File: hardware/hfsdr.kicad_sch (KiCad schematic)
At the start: 57 parts, among them J1 USB_C_Receptacle_USB2.0_16P, SW1 RST, SW2 BOOT0, SW4 RotaryEncoder_Switch, U3 CH32V30xRxTx

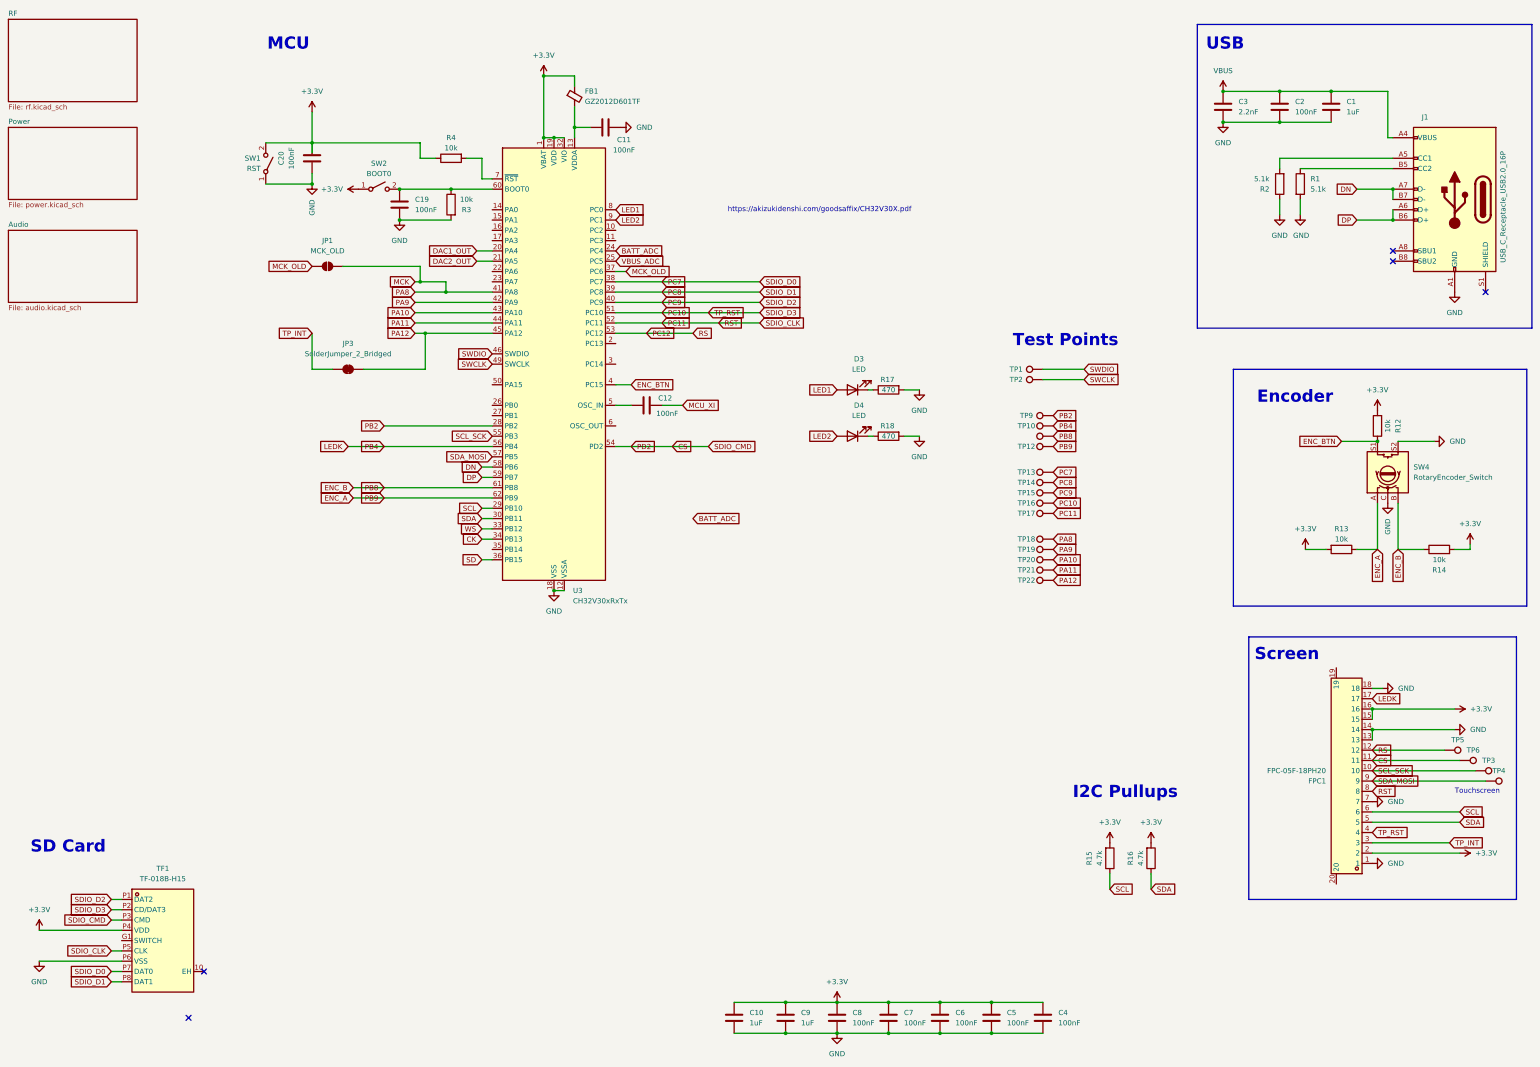
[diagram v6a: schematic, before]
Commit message: feat: tf card slot and screen rerouting
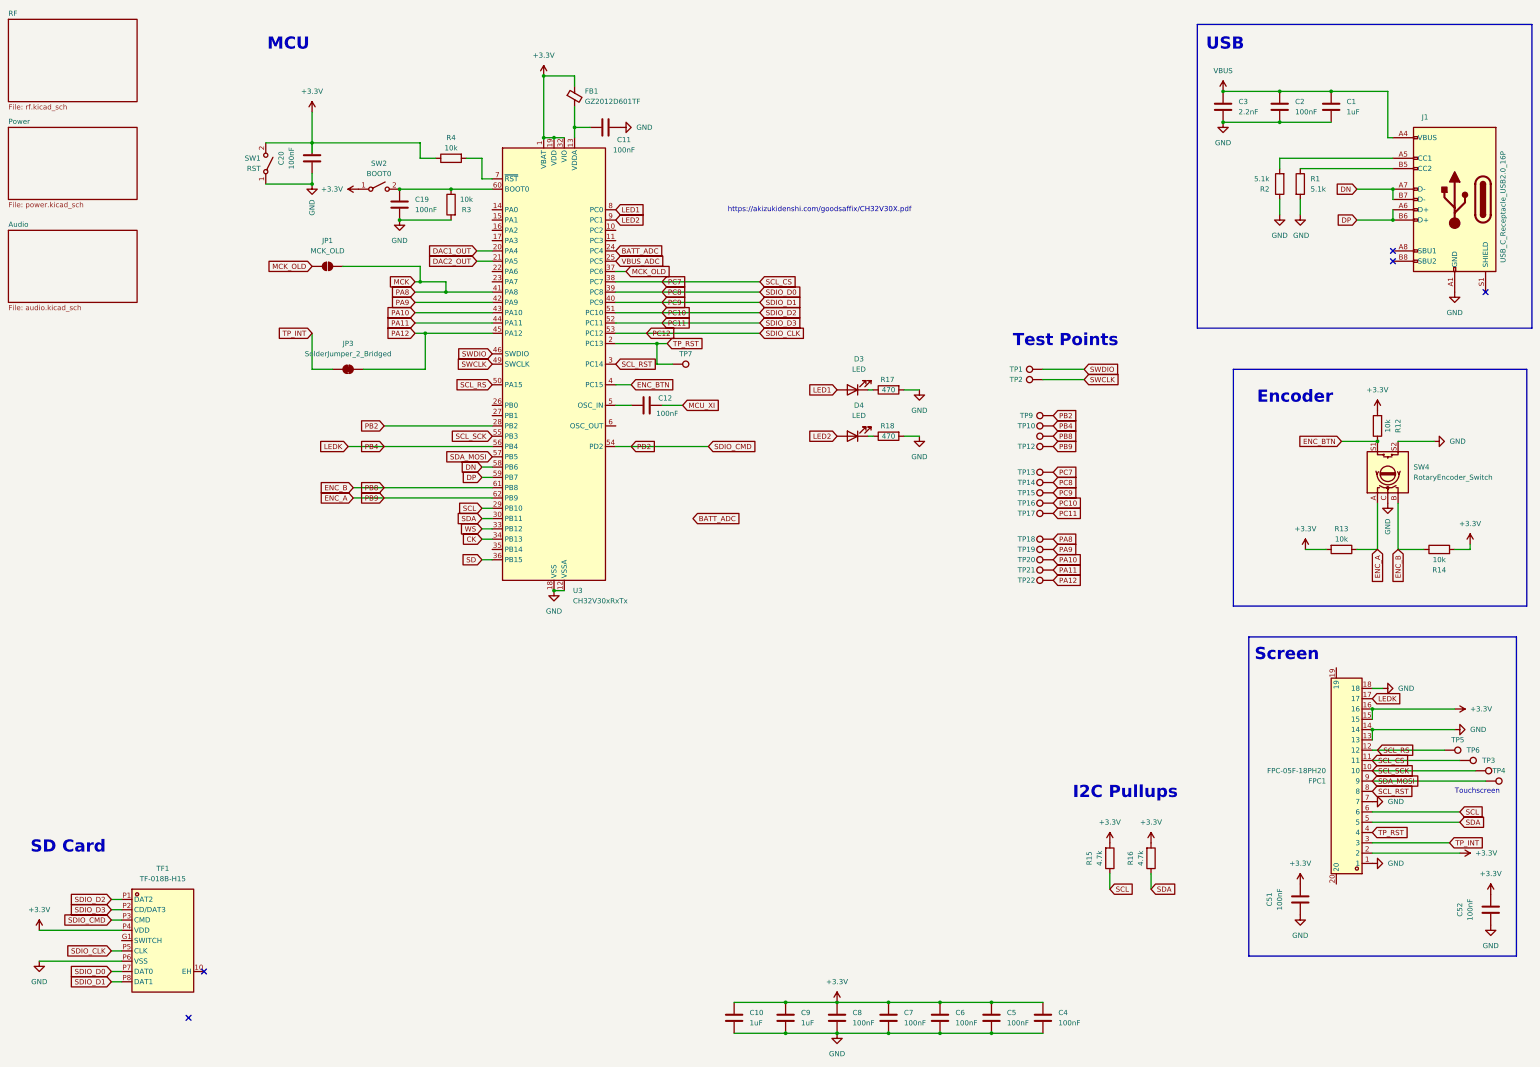
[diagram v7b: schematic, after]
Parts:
- added C51, C52: 100nF, Capacitor_SMD:C_0805_2012Metric_Pad1.18x1.45mm_HandSolder, symbol Device:C
- added TP7: TestPoint, TestPoint:TestPoint_Pad_1.0x1.0mm, symbol Connector:TestPoint
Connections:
- net +3.3V: now also C51.2, C52.2
- net GND: now also C51.1, C52.1
- net PC10: now also TF1.P1 (DAT2); no longer FPC1.4, TF1.P2 (CD/DAT3)
- net PC11: now also TF1.P2 (CD/DAT3); no longer FPC1.8, TF1.P5 (CLK)
- net PC12: now also TF1.P5 (CLK); no longer FPC1.12, TP5.1
- net PC7: now also FPC1.11, TP6.1; no longer TF1.P7 (DAT0)
- net PC8: now also TF1.P7 (DAT0); no longer TF1.P8 (DAT1)
- net PC9: now also TF1.P8 (DAT1); no longer TF1.P1 (DAT2)
- net TP_RST: now reaches U3.2 (PC13)
- net TP_RST: now also FPC1.4, TP7.1
- net SCL_RST: now reaches U3.3 (PC14)
- net SCL_RST: now also FPC1.8
- net SCL_RS: now reaches U3.50 (PA15)
- net SCL_RS: now also FPC1.12, TP5.1
- net CS renamed PD2
- net PD2: no longer FPC1.11, TP6.1

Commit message: Ready for production
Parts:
- added C53: 1uF, Capacitor_SMD:C_0805_2012Metric_Pad1.18x1.45mm_HandSolder, symbol Device:C
- added C54: 100nF, Capacitor_SMD:C_0805_2012Metric_Pad1.18x1.45mm_HandSolder, symbol Device:C
- C3: value 2.2nF -> 10nF
- R15, R16: value 4.7k -> 2k
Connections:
- net GND: now also C53.1, C54.1
- net VBUS: now also C53.2, C54.2
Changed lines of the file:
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@@
 	)
 	(junction
+		(at 345.44 30.48)
+		(diameter 0)
+		(color 0 0 0 0)
+	)
+	(junction
 		(at 332.74 38.1)
 		(diameter 0)
@@
 	(wire
 		(pts
+			(xy 332.74 30.48) (xy 345.44 30.48)
+		)
+		(stroke
+			(width 0)
+			(type default)
+		)
+	)
+	(wire
+		(pts
 			(xy 44.45 242.57) (xy 46.99 242.57)
 		)
@@
 			)
 		)
-		(property "Value" "4.7k"
+		(property "Value" "2k"
 			(at 298.45 227.33 90)
 			(effects
@@
 	)
 	(symbol
+		(lib_id "Device:C")
+		(at 345.44 34.29 0)
+		(unit 1)
+		(exclude_from_sim no)
+		(in_bom yes)
+		(on_board yes)
+		(dnp no)
+		(fields_autoplaced yes)
+		(property "Reference" "C53"
+			(at 349.25 33.0199 0)
+			(effects
+				(font
+					(size 1.27 1.27)
+				)
+				(justify left)
+			)
+		)
+		(property "Value" "1uF"
+			(at 349.25 35.5599 0)
+			(effects
+				(font
+					(size 1.27 1.27)
+				)
+				(justify left)
+			)
+		)
+		(property "Footprint" "Capacitor_SMD:C_0805_2012Metric_Pad1.18x1.45mm_HandSolder"
+			(at 346.4052 38.1 0)
+			(effects
+				(font
+					(size 1.27 1.27)
+				)
+				(hide yes)
+			)
+		)
+		(property "Datasheet" "~"
+			(at 345.44 34.29 0)
+			(effects
+				(font
+					(size 1.27 1.27)
+				)
+				(hide yes)
+			)
+		)
+		(property "Description" "Unpolarized capacitor"
+			(at 345.44 34.29 0)
+			(effects
+				(font
+					(size 1.27 1.27)
+				)
+				(hide yes)
+			)
+		)
+		(pin "2"
+		)
+		(pin "1"
+		)
+		(instances
+			(project "hfsdr"
+				(path "/a11445ed-c3bd-4d1c-a039-1c09b0dceab8"
+					(reference "C53")
+					(unit 1)
+				)
+			)
+		)
+	)
+	(symbol
 		(lib_id "Connector:TestPoint")
 		(at 276.86 120.65 90)
@@
 			)
 		)
-		(property "Value" "4.7k"
+		(property "Value" "2k"
 			(at 288.29 227.33 90)
 			(effects
@@
 	)
 	(symbol
+		(lib_id "power:GND")
+		(at 345.44 30.48 180)
+		(unit 1)
+		(exclude_from_sim no)
+		(in_bom yes)
+		(on_board yes)
+		(dnp no)
+		(fields_autoplaced yes)
+		(property "Reference" "#PWR089"
+			(at 345.44 24.13 0)
+			(effects
+				(font
+					(size 1.27 1.27)
+				)
+				(hide yes)
+			)
+		)
+		(property "Value" "GND"
+			(at 345.44 25.4 0)
+			(effects
+				(font
+					(size 1.27 1.27)
+				)
+			)
+		)
+		(property "Footprint" ""
+			(at 345.44 30.48 0)
+			(effects
+				(font
+					(size 1.27 1.27)
+				)
+				(hide yes)
+			)
+		)
+		(property "Datasheet" ""
+			(at 345.44 30.48 0)
+			(effects
+				(font
+					(size 1.27 1.27)
+				)
+				(hide yes)
+			)
+		)
+		(property "Description" "Power symbol creates a global label with name \"GND\" , ground"
+			(at 345.44 30.48 0)
+			(effects
+				(font
+					(size 1.27 1.27)
+				)
+				(hide yes)
+			)
+		)
+		(pin "1"
+		)
+		(instances
+			(project "hfsdr"
+				(path "/a11445ed-c3bd-4d1c-a039-1c09b0dceab8"
+					(reference "#PWR089")
+					(unit 1)
+				)
+			)
+		)
+	)
+	(symbol
 		(lib_id "Connector:TestPoint")
 		(at 276.86 151.13 90)
@@
 			)
 		)
-		(property "Value" "2.2nF"
+		(property "Value" "10nF"
 			(at 322.58 43.1799 0)
 			(effects
@@
 					(unit 1)
 				)
+			)
+		)
+	)
+	(symbol
+		(lib_id "Device:C")
+		(at 332.74 34.29 0)
+		(unit 1)
+		(exclude_from_sim no)
+		(in_bom yes)
+		(on_board yes)
+		(dnp no)
+		(fields_autoplaced yes)
+		(property "Reference" "C54"
+			(at 336.55 33.0199 0)
+			(effects
+				(font
+					(size 1.27 1.27)
+				)
+				(justify left)
+			)
+		)
+		(property "Value" "100nF"
+			(at 336.55 35.5599 0)
+			(effects
+				(font
+					(size 1.27 1.27)
+				)
+				(justify left)
+			)
+		)
+		(property "Footprint" "Capacitor_SMD:C_0805_2012Metric_Pad1.18x1.45mm_HandSolder"
+			(at 333.7052 38.1 0)
+			(effects
+				(font
+					(size 1.27 1.27)
+				)
+				(hide yes)
+			)
+		)
+		(property "Datasheet" "~"
+			(at 332.74 34.29 0)
+			(effects
+				(font
+					(size 1.27 1.27)
+				)
+				(hide yes)
+			)
+		)
+		(property "Description" "Unpolarized capacitor"
+			(at 332.74 34.29 0)
+			(effects
+				(font
+					(size 1.27 1.27)
+				)
+				(hide yes)
+			)
+		)
+		(pin "2"
+		)
+		(pin "1"
+		)
+		(instances
+			(project "hfsdr"
+				(path "/a11445ed-c3bd-4d1c-a039-1c09b0dceab8"
+					(reference "C54")
+					(unit 1)
+				)
